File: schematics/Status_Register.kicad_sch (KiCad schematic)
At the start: 13 parts, among them U1 74LS02, U2 74LS08, U3 74LS86, U4 74LS173

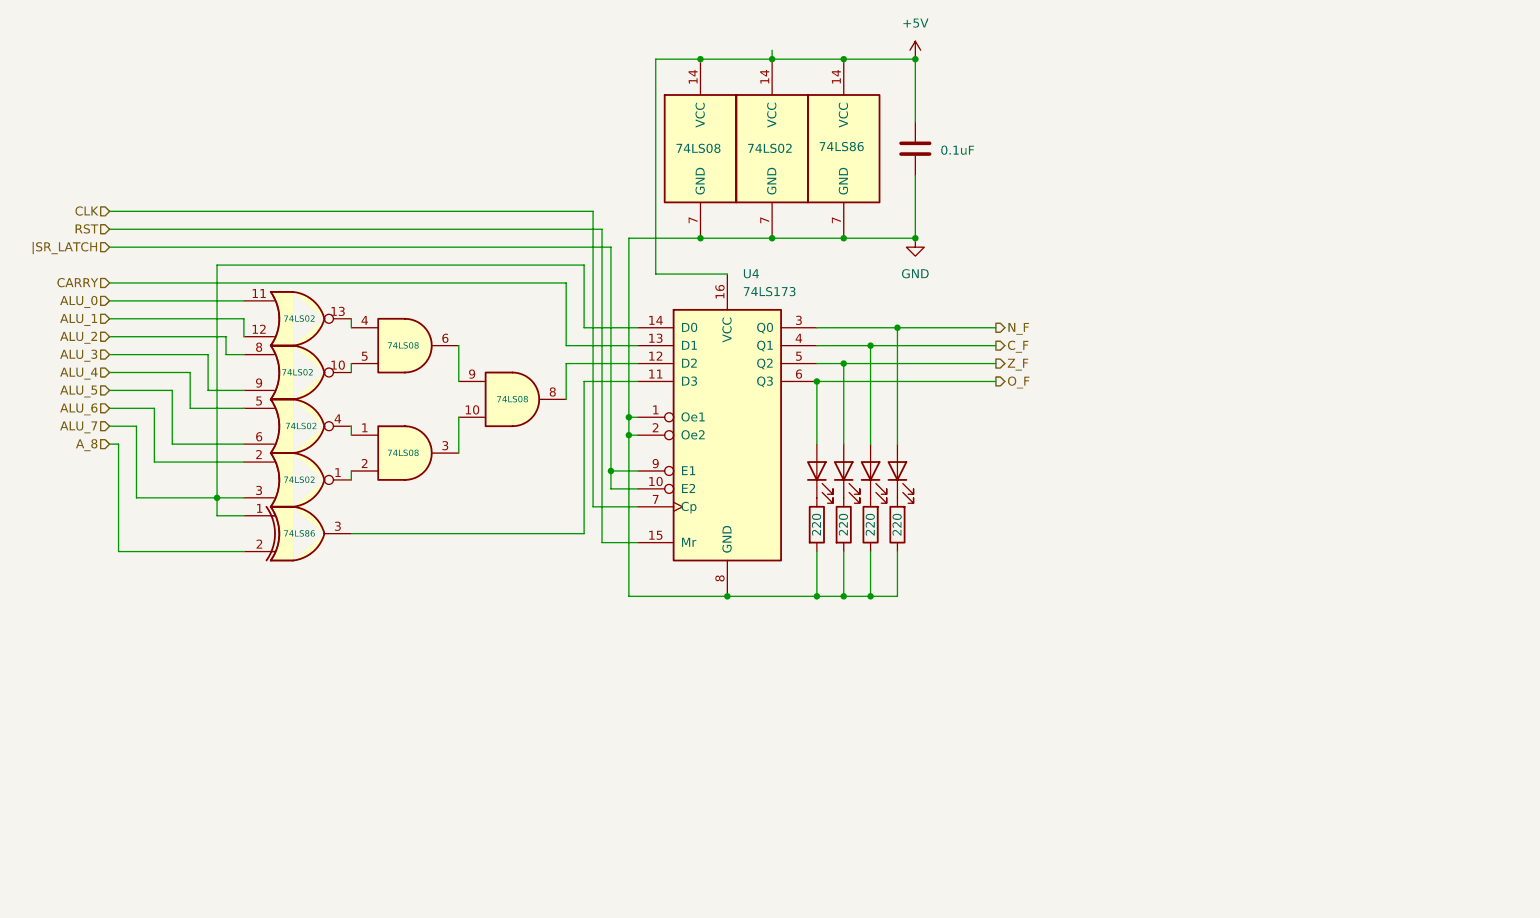
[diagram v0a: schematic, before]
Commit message: feat: updated electrical diagrams & individual part list
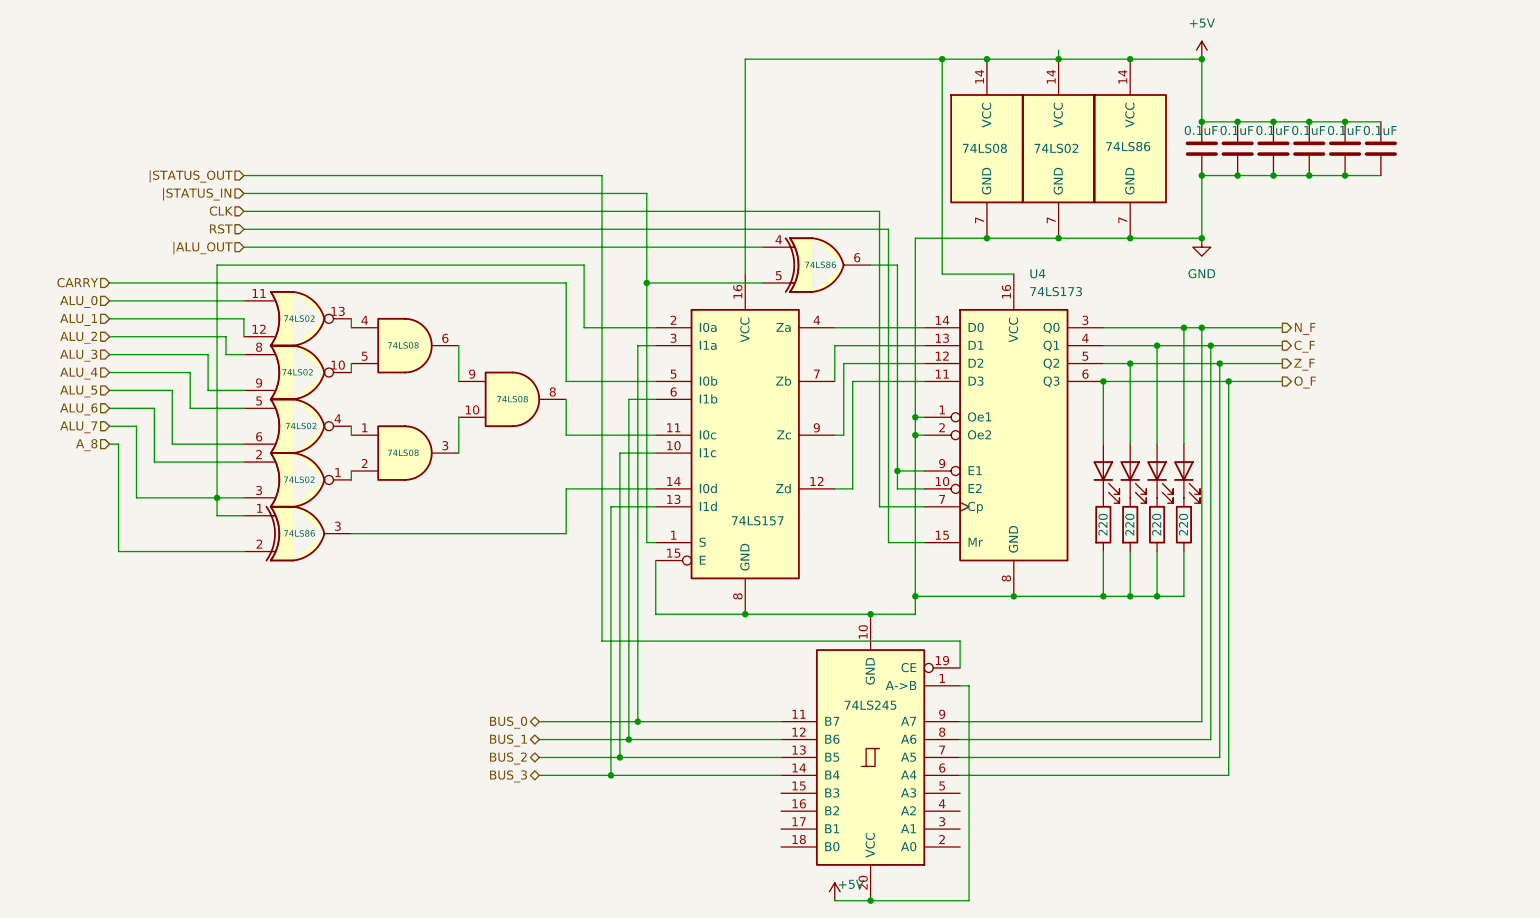
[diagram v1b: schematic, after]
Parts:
- added C2, C3, C4, C5, C6: 0.1uF, symbol Device:C
- added unit 2 of U3
- added U5: 74LS157, symbol 74xx:74LS157
- added U6: 74LS245, symbol 74xx:74LS245
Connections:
- net +5V: now also C2.1, C3.1, C4.1, C5.1, C6.1, U5.16 (VCC), U6.1 (A->B), U6.20 (VCC)
- net ALU_7: now also U5.2 (I0a); no longer U4.14 (D0)
- net CARRY: now also U5.5 (I0b); no longer U4.13 (D1)
- net C_F: now also U6.8 (A6)
- net GND: now also C2.2, C3.2, C4.2, C5.2, C6.2, U5.15 (E), U5.8 (GND), U6.10 (GND)
- net N_F: now also U6.9 (A7)
- net O_F: now also U6.6 (A4)
- net Z_F: now also U6.7 (A5)
- net at U2.8: now also U5.11 (I0c); no longer U4.12 (D2)
- net at U4.11 (D3): now also U5.12 (Zd); no longer U3.3
- net |SR_LATCH: no longer names the net of U4.10 (E2), U4.9 (E1)
- net |SR_LATCH: now also U3.6
- new net: U3.3, U5.14 (I0d)
- new net: U4.14 (D0), U5.4 (Za)
- new net: U4.13 (D1), U5.7 (Zb)
- new net: U4.12 (D2), U5.9 (Zc)
- new net BUS_0: U5.3 (I1a), U6.11 (B7)
- new net BUS_1: U5.6 (I1b), U6.12 (B6)
- new net BUS_2: U5.10 (I1c), U6.13 (B5)
- new net BUS_3: U5.13 (I1d), U6.14 (B4)
- new net |ALU_OUT: U3.4
- new net |STATUS_IN: U3.5, U5.1 (S)
- new net |STATUS_OUT: U6.19 (CE)
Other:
- moved on the sheet: U4

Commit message: Updated schematics and README
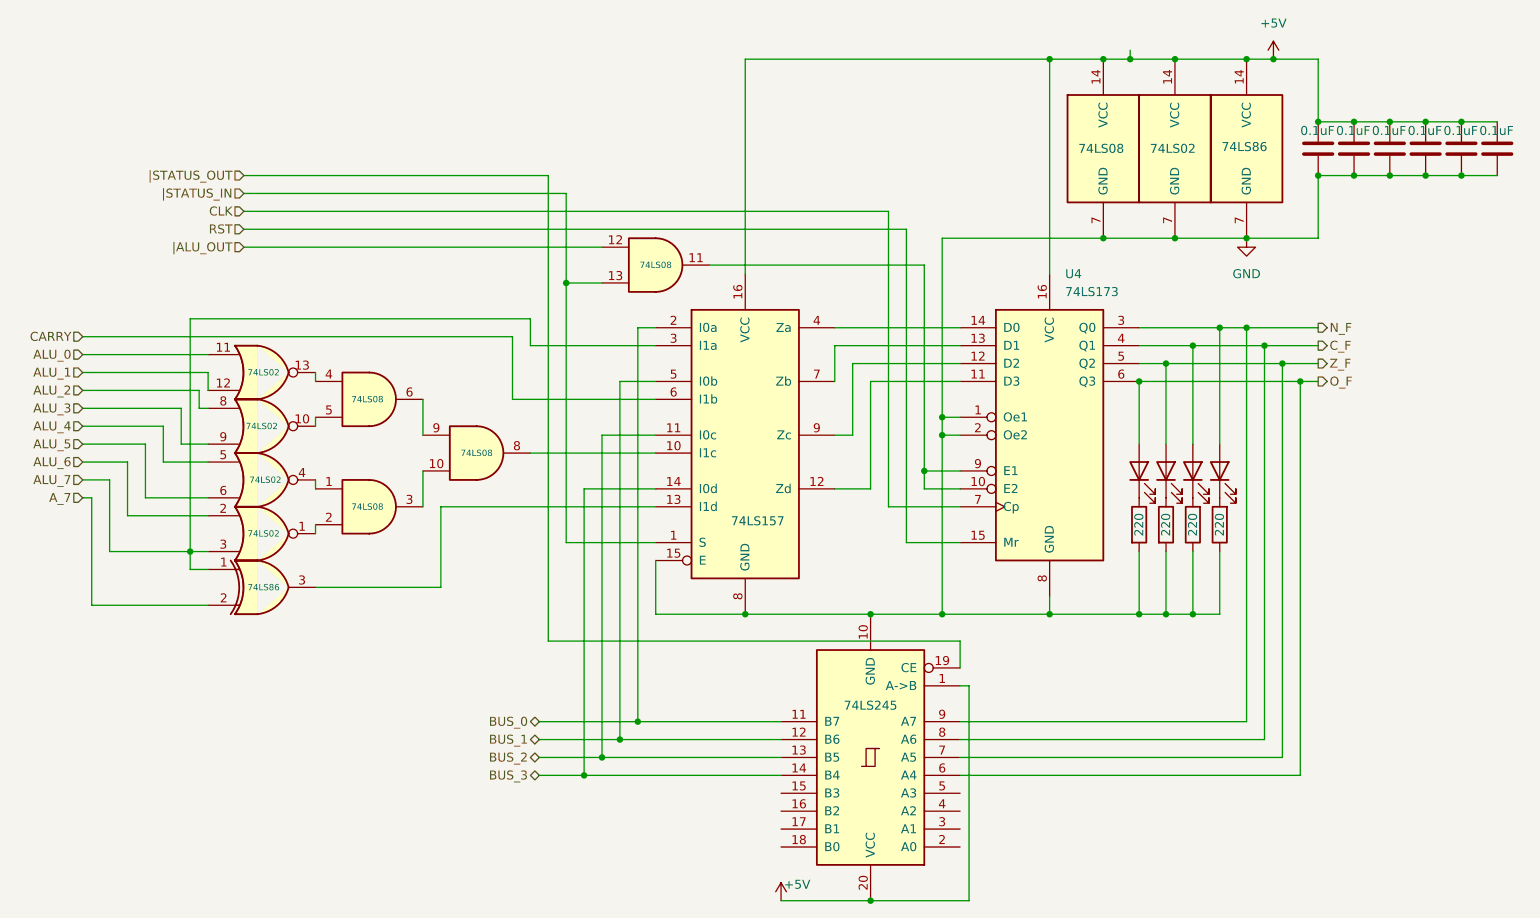
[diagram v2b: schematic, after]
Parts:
- removed unit 2 of U3
- added unit 4 of U2
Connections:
- net ALU_7: now also U5.3 (I1a); no longer U5.2 (I0a)
- net BUS_0: now also U5.2 (I0a); no longer U5.3 (I1a)
- net BUS_1: now also U5.5 (I0b); no longer U5.6 (I1b)
- net BUS_2: now also U5.11 (I0c); no longer U5.10 (I1c)
- net BUS_3: now also U5.14 (I0d); no longer U5.13 (I1d)
- net CARRY: now also U5.6 (I1b); no longer U5.5 (I0b)
- net |ALU_OUT: now also U2.12
- net |STATUS_IN: now also U2.13
- net at U2.8: now also U5.10 (I1c); no longer U5.11 (I0c)
- net at U3.3: now also U5.13 (I1d); no longer U5.14 (I0d)
- net at U4.10 (E2), U4.9 (E1): now also U2.11
- net A_8 renamed A_7
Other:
- moved on the sheet: U4
